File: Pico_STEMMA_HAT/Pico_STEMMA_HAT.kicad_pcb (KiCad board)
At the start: 2 copper layers, 58 x 67 mm, 46 parts, among them J1 Conn_01x20_Socket, J2 Conn_01x20_Socket, J3 SDCARD_MODULE, U1 Neopixel

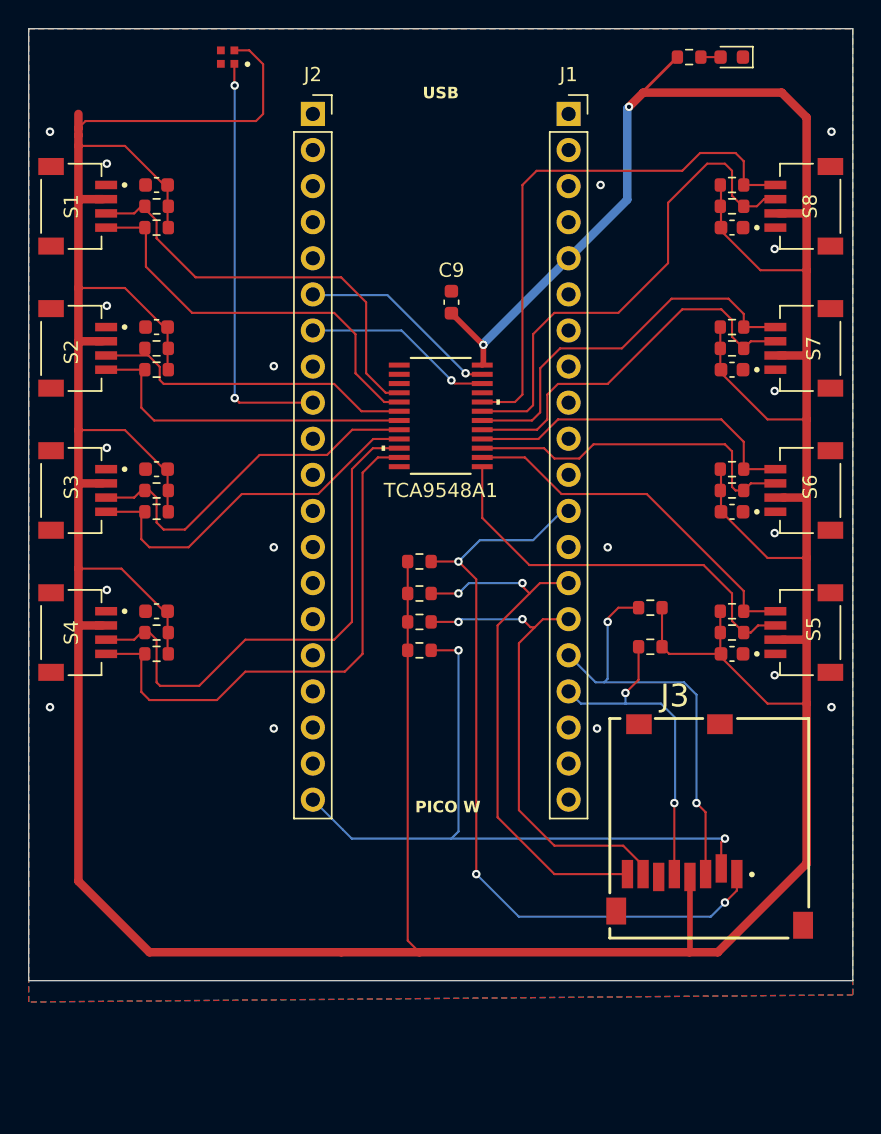
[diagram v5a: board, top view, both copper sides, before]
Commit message: Fix STEMMA GND Nets
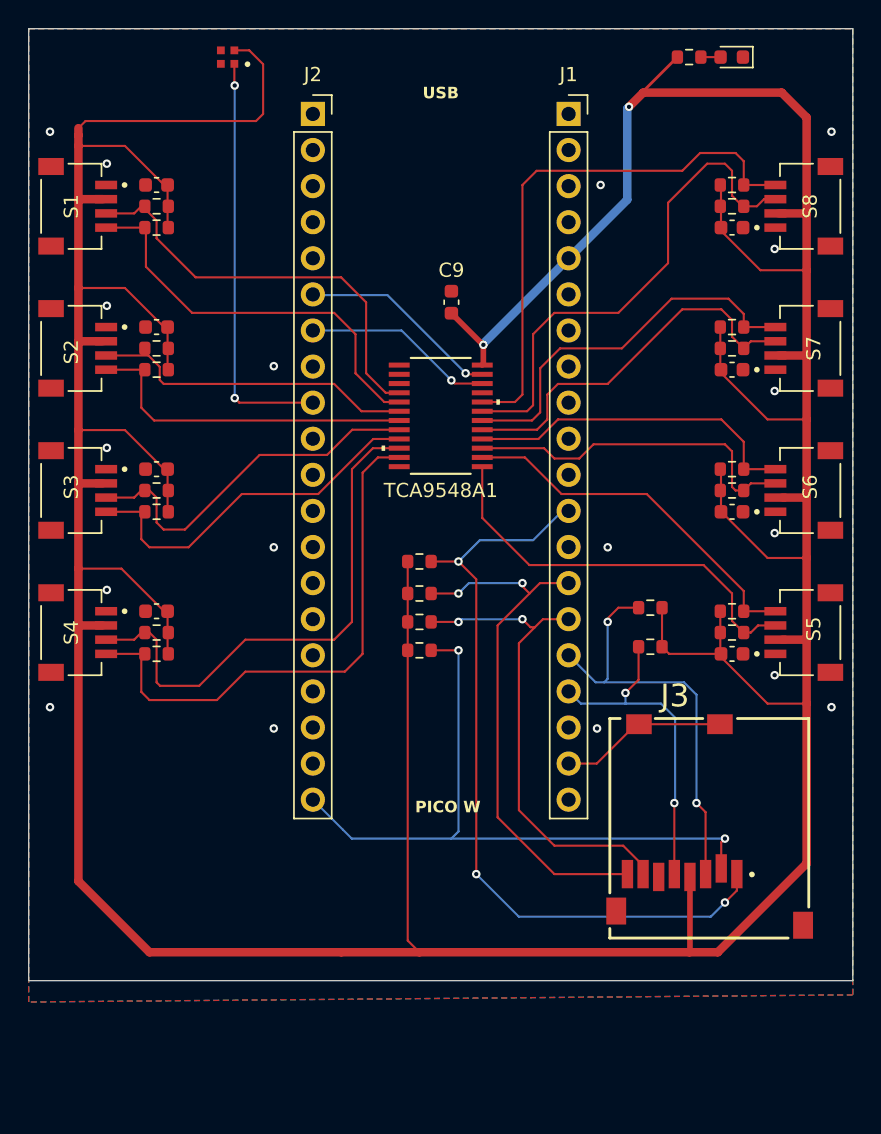
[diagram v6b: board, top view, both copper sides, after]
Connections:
- J1 pad 19: /GPIO17 -> /GPIO17/CARD_DETECT
- J3 pad 10: /CARD_DETECT -> /GPIO17/CARD_DETECT
- J3 pad 9: /CARD_DETECT -> /GPIO17/CARD_DETECT
- S1 pad S1: (no net) -> GND
- S1 pad S2: (no net) -> GND
- S2 pad S1: (no net) -> GND
- S2 pad S2: (no net) -> GND
- S3 pad S1: (no net) -> GND
- S3 pad S2: (no net) -> GND
- S4 pad S1: (no net) -> GND
- S4 pad S2: (no net) -> GND
- S5 pad S1: (no net) -> GND
- S5 pad S2: (no net) -> GND
- S6 pad S1: (no net) -> GND
- S6 pad S2: (no net) -> GND
- S7 pad S1: (no net) -> GND
- S7 pad S2: (no net) -> GND
- S8 pad S1: (no net) -> GND
- S8 pad S2: (no net) -> GND
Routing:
- net /GPIO17/CARD_DETECT: track 0.00 -> 11.8 mm
- net +3V3: track 361.8 -> 360.8 mm
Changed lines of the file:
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@@
 	(net 5 "/GPIO16{slash}DEC")
 	(net 6 "/GPIO28_ADC2")
-	(net 7 "/GPIO17")
+	(net 7 "/GPIO17{slash}CARD_DETECT")
 	(net 8 "/GPIO22{slash}DAT2")
 	(net 9 "/RUN")
@@
 	(net 54 "unconnected-(TCA9548A1-#RESET-Pad3)")
 	(net 55 "unconnected-(TCA9548A1-A2-Pad21)")
-	(net 56 "/CARD_DETECT")
-	(net 57 "unconnected-(U1-DOUT-Pad3)")
+	(net 56 "unconnected-(U1-DOUT-Pad3)")
 	(footprint "Resistor_SMD:R_0603_1608Metric"
 		(layer "F.Cu")
@@
 			(layers "*.Cu" "*.Mask")
 			(remove_unused_layers no)
-			(net 7 "/GPIO17")
+			(net 7 "/GPIO17{slash}CARD_DETECT")
 			(pinfunction "Pin_19")
-			(pintype "passive+no_connect")
+			(pintype "passive")
 		)
 		(pad "20" thru_hole oval
@@
 			)
 		)
-		(property "Description" "STEMMA QT"
+		(property "Description" "Port to connect the sensors, such as the magnetometers"
 			(at 0 0 90)
 			(layer "F.Fab")
@@
 			(size 1.2 1.8)
 			(layers "F.Cu" "F.Paste" "F.Mask")
+			(net 1 "GND")
+			(pinfunction "GND")
+			(pintype "power_in")
 			(solder_mask_margin 0.102)
 		)
@@
 			(size 1.2 1.8)
 			(layers "F.Cu" "F.Paste" "F.Mask")
+			(net 1 "GND")
+			(pinfunction "GND")
+			(pintype "power_in")
 			(solder_mask_margin 0.102)
 		)
-		(model "C:/Users/boccs/OneDrive/Desktop/FoldersFiles/REIMAGINED_3D_FILES_BLENDER/PRT-14417.step"
+		(model "C:/Users/boccs/OneDrive/Documents/GitHub/desk-project-stemma-hat/REIMAGINED_3D_FILES_BLENDER/PRT-14417.step"
 			(offset
 				(xyz 0 2 -0.3)
@@
 			)
 		)
-		(property "Description" "STEMMA QT"
+		(property "Description" "Port to connect the sensors, such as the magnetometers"
 			(at 0 0 90)
 			(layer "F.Fab")
@@
 			(size 1.2 1.8)
 			(layers "F.Cu" "F.Paste" "F.Mask")
+			(net 1 "GND")
+			(pinfunction "GND")
+			(pintype "power_in")
 			(solder_mask_margin 0.102)
 		)
@@
 			(size 1.2 1.8)
 			(layers "F.Cu" "F.Paste" "F.Mask")
+			(net 1 "GND")
+			(pinfunction "GND")
+			(pintype "power_in")
 			(solder_mask_margin 0.102)
 		)
-		(model "C:/Users/boccs/OneDrive/Desktop/FoldersFiles/REIMAGINED_3D_FILES_BLENDER/PRT-14417.step"
+		(model "C:/Users/boccs/OneDrive/Documents/GitHub/desk-project-stemma-hat/REIMAGINED_3D_FILES_BLENDER/PRT-14417.step"
 			(offset
 				(xyz 0 2 -0.3)
@@
 			(size 0.55 0.55)
 			(layers "F.Cu" "F.Paste" "F.Mask")
-			(net 57 "unconnected-(U1-DOUT-Pad3)")
+			(net 56 "unconnected-(U1-DOUT-Pad3)")
 			(pinfunction "DOUT")
 			(pintype "output+no_connect")
@@
 			(solder_mask_margin 0.102)
 		)
+		(model "C:/Users/boccs/OneDrive/Documents/GitHub/desk-project-stemma-hat/REIMAGINED_3D_FILES_BLENDER/4492.step"
+			(offset
+				(xyz 0 0 0)
+			)
+			(scale
+				(xyz 1 1 1)
+			)
+			(rotate
+				(xyz -90 0 0)
+			)
+		)
 	)
 	(footprint "Resistor_SMD:R_0603_1608Metric"
@@
 			)
 		)
-		(property "Description" "STEMMA QT"
+		(property "Description" "Port to connect the sensors, such as the magnetometers"
 			(at 0 0 90)
 			(layer "F.Fab")
@@
 			(size 1.2 1.8)
 			(layers "F.Cu" "F.Paste" "F.Mask")
+			(net 1 "GND")
+			(pinfunction "GND")
+			(pintype "power_in")
 			(solder_mask_margin 0.102)
 		)
@@
 			(size 1.2 1.8)
 			(layers "F.Cu" "F.Paste" "F.Mask")
+			(net 1 "GND")
+			(pinfunction "GND")
+			(pintype "power_in")
 			(solder_mask_margin 0.102)
 		)
-		(model "C:/Users/boccs/OneDrive/Desktop/FoldersFiles/REIMAGINED_3D_FILES_BLENDER/PRT-14417.step"
+		(model "C:/Users/boccs/OneDrive/Documents/GitHub/desk-project-stemma-hat/REIMAGINED_3D_FILES_BLENDER/PRT-14417.step"
 			(offset
 				(xyz 0 2 -0.3)
@@
 			)
 		)
-		(property "Description" "STEMMA QT"
+		(property "Description" "Port to connect the sensors, such as the magnetometers"
 			(at 0 0 90)
 			(layer "F.Fab")
@@
 			(size 1.2 1.8)
 			(layers "F.Cu" "F.Paste" "F.Mask")
+			(net 1 "GND")
+			(pinfunction "GND")
+			(pintype "power_in")
 			(solder_mask_margin 0.102)
 		)
@@
 			(size 1.2 1.8)
 			(layers "F.Cu" "F.Paste" "F.Mask")
+			(net 1 "GND")
+			(pinfunction "GND")
+			(pintype "power_in")
 			(solder_mask_margin 0.102)
 		)
-		(model "C:/Users/boccs/OneDrive/Desktop/FoldersFiles/REIMAGINED_3D_FILES_BLENDER/PRT-14417.step"
+		(model "C:/Users/boccs/OneDrive/Documents/GitHub/desk-project-stemma-hat/REIMAGINED_3D_FILES_BLENDER/PRT-14417.step"
 			(offset
 				(xyz 0 2 -0.3)
@@
 			)
 		)
-		(property "Description" "STEMMA QT"
+		(property "Description" "Port to connect the sensors, such as the magnetometers"
 			(at 0 0 90)
 			(layer "F.Fab")
@@
 			(size 1.2 1.8)
 			(layers "F.Cu" "F.Paste" "F.Mask")
+			(net 1 "GND")
+			(pinfunction "GND")
+			(pintype "power_in")
 			(solder_mask_margin 0.102)
 		)
@@
 			(size 1.2 1.8)
 			(layers "F.Cu" "F.Paste" "F.Mask")
+			(net 1 "GND")
+			(pinfunction "GND")
+			(pintype "power_in")
 			(solder_mask_margin 0.102)
 		)
-		(model "C:/Users/boccs/OneDrive/Desktop/FoldersFiles/REIMAGINED_3D_FILES_BLENDER/PRT-14417.step"
+		(model "C:/Users/boccs/OneDrive/Documents/GitHub/desk-project-stemma-hat/REIMAGINED_3D_FILES_BLENDER/PRT-14417.step"
 			(offset
 				(xyz 0 2 -0.3)
@@
 			)
 		)
-		(property "Description" "STEMMA QT"
+		(property "Description" "Port to connect the sensors, such as the magnetometers"
 			(at 0 0 90)
 			(layer "F.Fab")
@@
 			(size 1.2 1.8)
 			(layers "F.Cu" "F.Paste" "F.Mask")
+			(net 1 "GND")
+			(pinfunction "GND")
+			(pintype "power_in")
 			(solder_mask_margin 0.102)
 		)
@@
 			(size 1.2 1.8)
 			(layers "F.Cu" "F.Paste" "F.Mask")
+			(net 1 "GND")
+			(pinfunction "GND")
+			(pintype "power_in")
 			(solder_mask_margin 0.102)
 		)
-		(model "C:/Users/boccs/OneDrive/Desktop/FoldersFiles/REIMAGINED_3D_FILES_BLENDER/PRT-14417.step"
+		(model "C:/Users/boccs/OneDrive/Documents/GitHub/desk-project-stemma-hat/REIMAGINED_3D_FILES_BLENDER/PRT-14417.step"
 			(offset
 				(xyz 0 2 -0.3)
@@
 			(size 1.8 1.4)
 			(layers "F.Cu" "F.Paste" "F.Mask")
-			(net 56 "/CARD_DETECT")
+			(net 7 "/GPIO17{slash}CARD_DETECT")
 			(pinfunction "CD1")
 			(pintype "passive")
@@
 			(size 1.8 1.4)
 			(layers "F.Cu" "F.Paste" "F.Mask")
-			(net 56 "/CARD_DETECT")
+			(net 7 "/GPIO17{slash}CARD_DETECT")
 			(pinfunction "CD2")
 			(pintype "passive")
@@
 			)
 		)
+		(model "C:/Users/boccs/OneDrive/Documents/GitHub/desk-project-stemma-hat/REIMAGINED_3D_FILES_BLENDER/MEM2061-01-188-00-A_REVA.step"
+			(offset
+				(xyz 0 0 0)
+			)
+			(scale
+				(xyz 1 1 1)
+			)
+			(rotate
+				(xyz -90 0 0)
+			)
+		)
 	)
 	(footprint "Resistor_SMD:R_0603_1608Metric"
@@
 			)
 		)
-		(property "Description" "STEMMA QT"
+		(property "Description" "Port to connect the sensors, such as the magnetometers"
 			(at 0 0 90)
 			(layer "F.Fab")
@@
 			(size 1.2 1.8)
 			(layers "F.Cu" "F.Paste" "F.Mask")
+			(net 1 "GND")
+			(pinfunction "GND")
+			(pintype "power_in")
 			(solder_mask_margin 0.102)
 		)
@@
 			(size 1.2 1.8)
 			(layers "F.Cu" "F.Paste" "F.Mask")
+			(net 1 "GND")
+			(pinfunction "GND")
+			(pintype "power_in")
 			(solder_mask_margin 0.102)
 		)
-		(model "C:/Users/boccs/OneDrive/Desktop/FoldersFiles/REIMAGINED_3D_FILES_BLENDER/PRT-14417.step"
+		(model "C:/Users/boccs/OneDrive/Documents/GitHub/desk-project-stemma-hat/REIMAGINED_3D_FILES_BLENDER/PRT-14417.step"
 			(offset
 				(xyz 0 2 -0.3)
@@
 			)
 		)
-		(property "Description" "STEMMA QT"
+		(property "Description" "Port to connect the sensors, such as the magnetometers"
 			(at 0 0 90)
 			(layer "F.Fab")
@@
 			(size 1.2 1.8)
 			(layers "F.Cu" "F.Paste" "F.Mask")
+			(net 1 "GND")
+			(pinfunction "GND")
+			(pintype "power_in")
 			(solder_mask_margin 0.102)
 		)
@@
 			(size 1.2 1.8)
 			(layers "F.Cu" "F.Paste" "F.Mask")
+			(net 1 "GND")
+			(pinfunction "GND")
+			(pintype "power_in")
 			(solder_mask_margin 0.102)
 		)
-		(model "C:/Users/boccs/OneDrive/Desktop/FoldersFiles/REIMAGINED_3D_FILES_BLENDER/PRT-14417.step"
+		(model "C:/Users/boccs/OneDrive/Documents/GitHub/desk-project-stemma-hat/REIMAGINED_3D_FILES_BLENDER/PRT-14417.step"
 			(offset
 				(xyz 0 2 -0.3)
@@
 			(layer "F.Fab")
 		)
-		(fp_text user "*"
-			(at -1.8669 -3.8735 0)
+		(fp_text user "${REFERENCE}"
+			(at 0 5.25 0)
 			(unlocked yes)
 			(layer "F.Fab")
@@
 			)
 		)
-		(fp_text user "${REFERENCE}"
-			(at 0 5.25 0)
+		(fp_text user "*"
+			(at -1.8669 -3.8735 0)
 			(unlocked yes)
 			(layer "F.Fab")
@@
 			)
 		)
-		(model "/Users/martin.armand27/Documents/GitHub/desk-project-pico-stemma-hat/REIMAGINED_3D_FILES_BLENDER/PW0024A.stp"
+		(model "C:/Users/boccs/OneDrive/Documents/GitHub/desk-project-stemma-hat/REIMAGINED_3D_FILES_BLENDER/PW0024A.stp"
 			(offset
 				(xyz 0 0 0)
@@
 	)
 	(segment
-		(start 124.5 79.5)
-		(end 124.5 78.5)
-		(width 0.6)
-		(layer "F.Cu")
-		(net 2)
-	)
-	(segment
 		(start 124.5 80)
 		(end 124.5 79.5)
@@
 	)
 	(segment
+		(start 160.98 124.22)
+		(end 159 124.22)
+		(width 0.15)
+		(layer "F.Cu")
+		(net 7)
+	)
+	(segment
+		(start 163.95 121.45)
+		(end 163.75 121.45)
+		(width 0.15)
+		(layer "F.Cu")
+		(net 7)
+	)
+	(segment
+		(start 163.75 121.45)
+		(end 160.98 124.22)
+		(width 0.15)
+		(layer "F.Cu")
+		(net 7)
+	)
+	(segment
+		(start 169.65 121.45)
+		(end 163.95 121.45)
+		(width 0.15)
+		(layer "F.Cu")
+		(net 7)
+	)
+	(segment
